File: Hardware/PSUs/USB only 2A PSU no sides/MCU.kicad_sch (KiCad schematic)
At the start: 19 parts, among them J12 USB, U3 STM32G071GBUxN, U5 THVD1420DRLR, U6 CH32X035G8U6

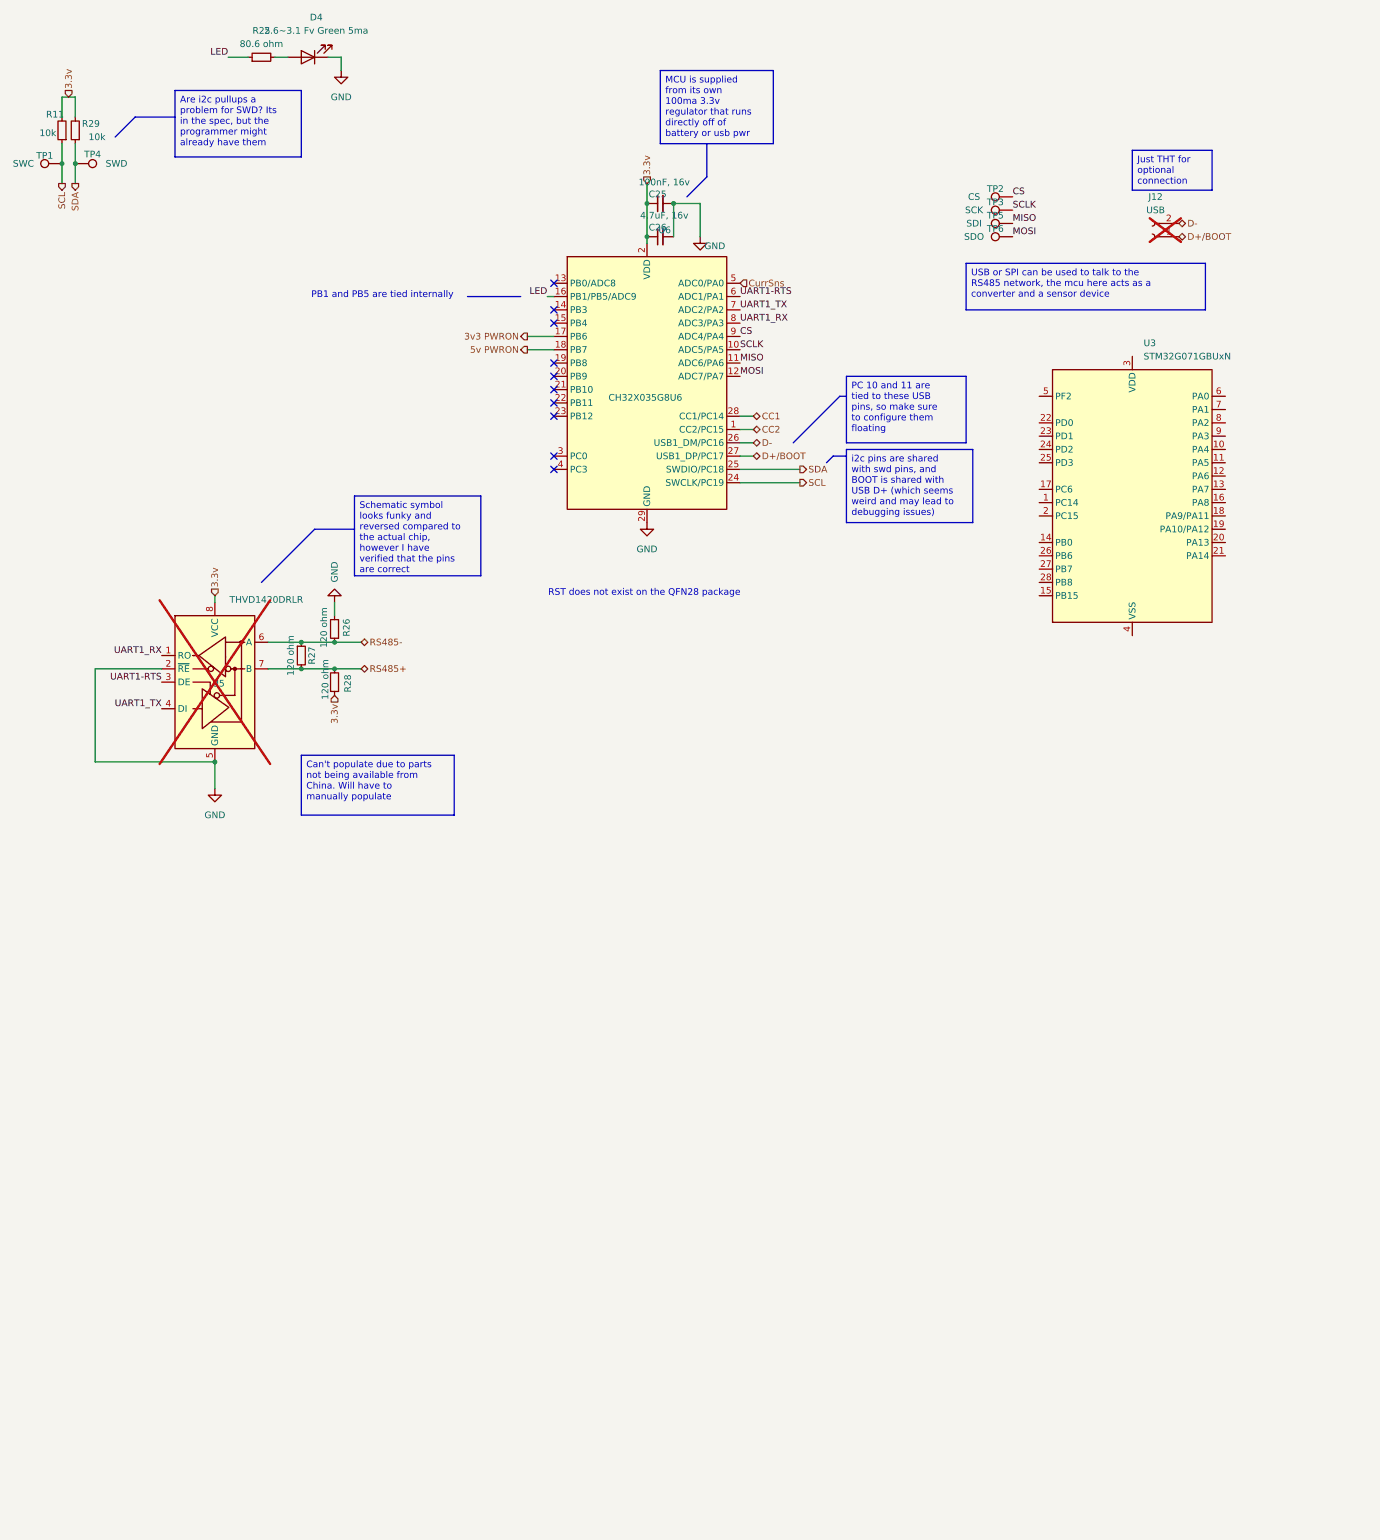
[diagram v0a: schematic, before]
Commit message: Started replacement of MCU with STM32
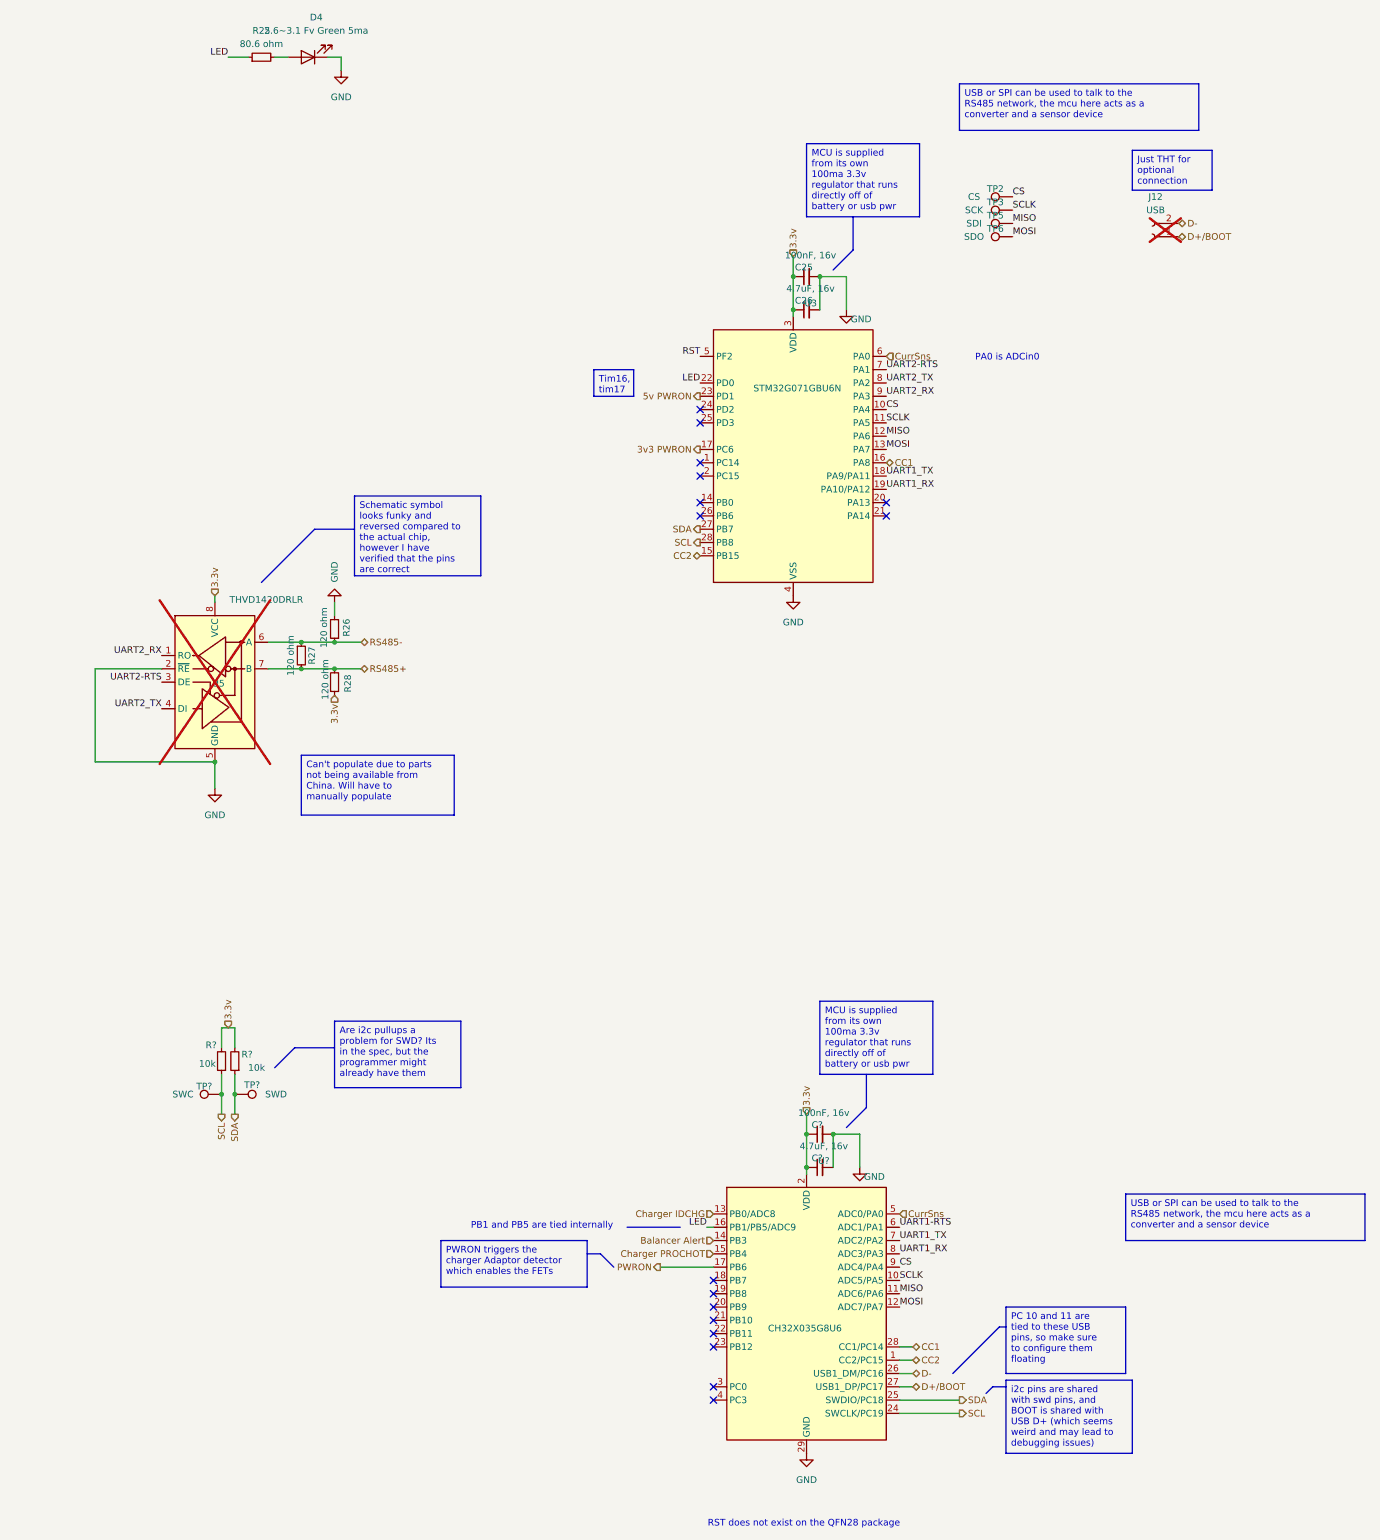
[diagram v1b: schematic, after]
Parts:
- U3: value STM32G071GBUxN -> STM32G071GBU6N
- renumbered C25 to C?, C26 to C?, R11 to R?, R29 to R?, TP1 to TP?, TP4 to TP?, U6 to U?
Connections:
- net 3.3v: now also U3.3 (VDD)
- net 3v3 PWRON: now also U3.17 (PC6); no longer U?.17 (PB6)
- net 5v PWRON: now also U3.23 (PD1); no longer U?.18 (PB7)
- net CC1: now also U3.16 (PA8)
- net CC2: now also U3.15 (PB15)
- net CS: now also U3.10 (PA4)
- net CurrSns: now also U3.6 (PA0)
- net GND: now also U3.4 (VSS)
- net LED: now also U3.22 (PD0)
- net MISO: now also U3.12 (PA6)
- net MOSI: now also U3.13 (PA7)
- net SCL: now also U3.28 (PB8)
- net SCLK: now also U3.11 (PA5)
- net SDA: now also U3.27 (PB7)
- net UART1-RTS: no longer U5.3 (DE)
- net UART1_RX: now also U3.19 (PA10/PA12); no longer U5.1 (RO)
- net UART1_TX: now also U3.18 (PA9/PA11); no longer U5.4 (DI)
- net Charger IDCHG: now reaches U?.13 (PB0/ADC8)
- net Balancer Alert: now reaches U?.14 (PB3)
- net Charger PROCHOT: now reaches U?.15 (PB4)
- net RST: now reaches U3.5 (PF2)
- net UART2-RTS: now reaches U3.7 (PA1)
- net UART2-RTS: now also U5.3 (DE)
- net UART2_TX: now reaches U3.8 (PA2)
- net UART2_TX: now also U5.4 (DI)
- net UART2_RX: now reaches U3.9 (PA3)
- net UART2_RX: now also U5.1 (RO)
- new net PWRON: U?.17 (PB6)
- no-connect marks 10 -> 16
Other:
- note added: "PA0 is ADCin0"
- moved on the sheet: C25, C26, R?, TP?, U3, U?

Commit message: Finished schematic, started arrangement
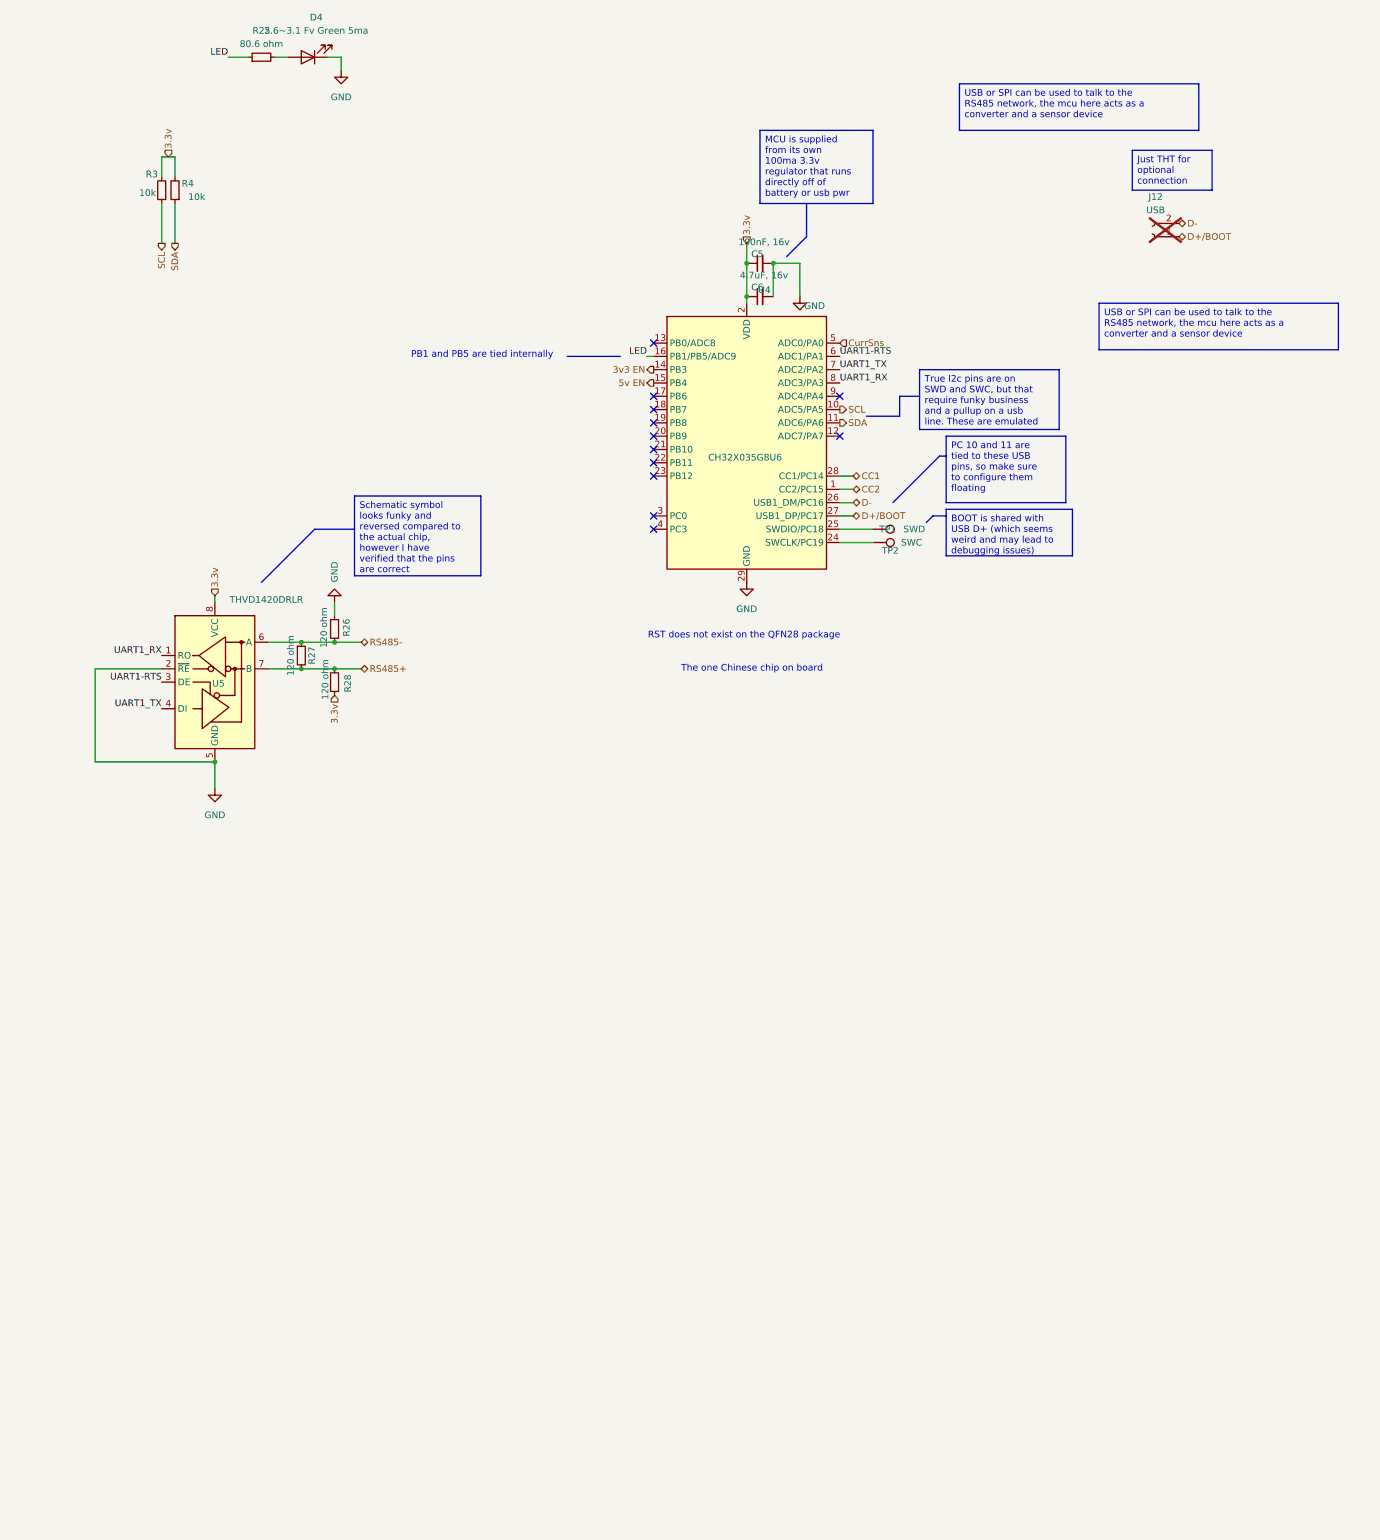
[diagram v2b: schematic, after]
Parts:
- removed TP2: CS, TestPoint:TestPoint_Pad_D1.0mm, symbol Connector:TestPoint
- removed TP3: SCK, TestPoint:TestPoint_Pad_D1.0mm, symbol Connector:TestPoint
- removed TP5: SDI, TestPoint:TestPoint_Pad_D1.0mm, symbol Connector:TestPoint
- removed TP6: SDO, TestPoint:TestPoint_Pad_D1.0mm, symbol Connector:TestPoint
- removed U3: STM32G071GBU6N, Package_DFN_QFN:QFN-28_4x4mm_P0.5mm, symbol MCU_ST_STM32G0:STM32G071GBUxN
- U4: renamed from U?; footprint Package_DFN_QFN:QFN-28-1EP_4x4mm_P0.4mm_EP2.8x2.8mm -> Package_DFN_QFN:QFN-28-1EP_4x4mm_P0.4mm_EP2.4x2.4mm
- U5: now fitted
- gave numbers to parts that had none: 6
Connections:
- net MISO is gone; now on net SDA: U4.11 (ADC6/PA6)
- net SCLK is gone; now on net SCL: U4.10 (ADC5/PA5)
- net UART2-RTS is gone; now on net UART1-RTS: U5.3 (DE)
- net UART2_RX is gone; now on net UART1_RX: U5.1 (RO)
- net UART2_TX is gone; now on net UART1_TX: U5.4 (DI)
- net SCL: no longer TP2.1, U4.24 (SWCLK/PC19)
- net SDA: no longer TP1.1, U4.25 (SWDIO/PC18)
- net Balancer Alert renamed 3v3 EN
- net CS: no longer names the net of U4.9 (ADC4/PA4)
- net Charger IDCHG: no longer names the net of U4.13 (PB0/ADC8)
- net Charger PROCHOT renamed 5v EN
- net MOSI: no longer names the net of U4.12 (ADC7/PA7)
- net PWRON: no longer names the net of U4.17 (PB6)
- new net: TP2.1, U4.24 (SWCLK/PC19)
- new net: TP1.1, U4.25 (SWDIO/PC18)
- no-connect marks 16 -> 12
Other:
- note added: "The one Chinese chip on board"
- note removed: "PA0 is ADCin0"
- moved on the sheet: C5, C6, R3, R4, TP1, TP2, U4

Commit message: Moved current sense to PSU schematic
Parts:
- C5: footprint Capacitor_SMD:C_0402_1005Metric -> Capacitor_SMD:C_0805_2012Metric
- C6: footprint Capacitor_SMD:C_0603_1608Metric -> Capacitor_SMD:C_0805_2012Metric
- R25, R26, R27, R28, R3, R4: footprint Resistor_SMD:R_0402_1005Metric -> Resistor_SMD:R_0805_2012Metric
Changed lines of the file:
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@@
 			)
 		)
-		(property "Footprint" "Resistor_SMD:R_0402_1005Metric"
+		(property "Footprint" "Resistor_SMD:R_0805_2012Metric"
 			(at 48.26 55.88 0)
 			(effects
@@
 			)
 		)
-		(property "Footprint" "Resistor_SMD:R_0402_1005Metric"
+		(property "Footprint" "Resistor_SMD:R_0805_2012Metric"
 			(at 74.93 144.78 0)
 			(effects
@@
 			)
 		)
-		(property "Footprint" "Resistor_SMD:R_0402_1005Metric"
+		(property "Footprint" "Resistor_SMD:R_0805_2012Metric"
 			(at 81.28 139.7 0)
 			(effects
@@
 			)
 		)
-		(property "Footprint" "Resistor_SMD:R_0402_1005Metric"
+		(property "Footprint" "Resistor_SMD:R_0805_2012Metric"
 			(at 67.31 30.48 0)
 			(effects
@@
 			)
 		)
-		(property "Footprint" "Capacitor_SMD:C_0402_1005Metric"
+		(property "Footprint" "Capacitor_SMD:C_0805_2012Metric"
 			(at 162.56 69.85 0)
 			(effects
@@
 			)
 		)
-		(property "Footprint" "Resistor_SMD:R_0402_1005Metric"
+		(property "Footprint" "Resistor_SMD:R_0805_2012Metric"
 			(at 81.28 149.86 0)
 			(effects
@@
 			)
 		)
-		(property "Footprint" "Resistor_SMD:R_0402_1005Metric"
+		(property "Footprint" "Resistor_SMD:R_0805_2012Metric"
 			(at 50.8 55.88 0)
 			(effects
@@
 			)
 		)
-		(property "Footprint" "Capacitor_SMD:C_0603_1608Metric"
+		(property "Footprint" "Capacitor_SMD:C_0805_2012Metric"
 			(at 162.56 76.2 0)
 			(effects
